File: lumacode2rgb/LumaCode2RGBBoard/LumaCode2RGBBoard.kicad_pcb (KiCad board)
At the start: 2 copper layers, 50 x 60 mm, 74 parts, among them J4 USB_B_Micro, SW1 SW_Push, U1 TVP7002, U10 AP2127K-3.3, U11 74AHC595, U12 74AHC595, U2 AP2127K-3.3, U3 AP2127K-3.3, U4 AP2127K-1.9, U5 AP2127K-1.9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

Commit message: PCB layout
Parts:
- removed C20: 10uF, Capacitor_SMD:C_0805_2012Metric
- added JPICKIT2: Conn_01x02, Connector_PinHeader_2.54mm:PinHeader_1x02_P2.54mm_Vertical, F.Cu at (160.2, 51.4)
- JPICKIT1: value Conn_01x05 -> Conn_01x03; footprint Connector_PinHeader_2.54mm:PinHeader_1x05_P2.54mm_Vertical -> Connector_PinHeader_2.54mm:PinHeader_1x03_P2.54mm_Vertical
- R10, R11, R12, R13, R14, R15, R16, R17, R18, R19, R20, R21, R22, R23, R24, R25, R6, R7, R8, R9: footprint Resistor_SMD:R_0805_2012Metric -> Resistor_SMD:R_0603_1608Metric
- moved C23 131.6 mm to (155.0, 56.8), turned to 180 degrees
- moved C26 120.9 mm to (147.0, 49.8)
- moved R5 110.5 mm to (162.0, 66.4)
- moved C25 109.1 mm to (150.8, 49.2)
- moved U9 106.4 mm to (150.8, 52.5), turned to 90 degrees
- moved C24 96.8 mm to (147.0, 56.5), turned to 180 degrees
- moved R19 92.6 mm to (140.0, 46.0), turned to 90 degrees
- moved R15 92.0 mm to (142.0, 43.0), turned to 180 degrees
- moved R8 89.1 mm to (134.0, 35.5), turned to 180 degrees
- moved R14 88.0 mm to (134.0, 40.5), turned to 180 degrees
- moved R9 86.0 mm to (142.0, 38.0), turned to 180 degrees
- moved R12 85.7 mm to (142.0, 40.5), turned to 180 degrees
- moved R24 85.4 mm to (130.0, 40.5)
- moved R6 85.3 mm to (142.0, 35.5), turned to 180 degrees
- moved R11 84.5 mm to (134.0, 38.0), turned to 180 degrees
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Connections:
- JPICKIT1 pad 1: /Processing/VPP -> /Processing/ICSPCLK
- JPICKIT1 pad 2: +3.3V -> GND
- JPICKIT1 pad 3: GND -> /Processing/ICSPDAT
- R10 pad 2: /Processing/RED -> /Processing/BLUE
- R11 pad 2: /Processing/RED -> /Processing/BLUE
- R17 pad 2: /Processing/BLUE -> /Processing/RED
- R18 pad 2: /Processing/BLUE -> /Processing/RED
- R19 pad 2: /Processing/BLUE -> /Processing/RED
- R20 pad 2: /Processing/BLUE -> /Processing/RED
- R21 pad 2: /Processing/BLUE -> /Processing/RED
- R23 pad 2: /Processing/RED -> /Processing/BLUE
- R25 pad 2: /Processing/BLUE -> /Processing/RED
- R7 pad 2: /Processing/RED -> /Processing/BLUE
- R8 pad 2: /Processing/RED -> /Processing/BLUE
- R9 pad 2: /Processing/RED -> /Processing/BLUE
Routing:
- net +5V: track 0.00 -> 119.8 mm, vias 0 -> 8
- net GND: track 0.00 -> 85.5 mm, vias 0 -> 39
- net Net-(JBOTTOM2-Pad10): track 0.00 -> 51.3 mm, vias 0 -> 2
- net /Input/HSOUT: track 0.00 -> 50.6 mm
- net /Input/VSOUT: track 0.00 -> 50.0 mm
- net /Input/IOVDD: track 0.00 -> 49.3 mm, vias 0 -> 2
- net /Input/AUDIO_LEFT: track 0.00 -> 39.0 mm, vias 0 -> 2
- net Net-(C7-Pad1): track 0.00 -> 38.5 mm
- net /Processing/BLUE: track 0.00 -> 38.1 mm, vias 0 -> 1
- net /Input/SCL: track 0.00 -> 35.6 mm, vias 0 -> 2
- net /Input/SDA: track 0.00 -> 33.5 mm, vias 0 -> 2
- net /Input/AVDD: track 0.00 -> 26.5 mm, vias 0 -> 3
- net /Input/DVDD: track 0.00 -> 24.2 mm, vias 0 -> 2
- net /Processing/GREEN: track 0.00 -> 24.0 mm
- net /Input/A33VDD: track 0.00 -> 21.5 mm
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- added copper zone on B.Cu, net GND
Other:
- outline, holes or cut-outs redrawn

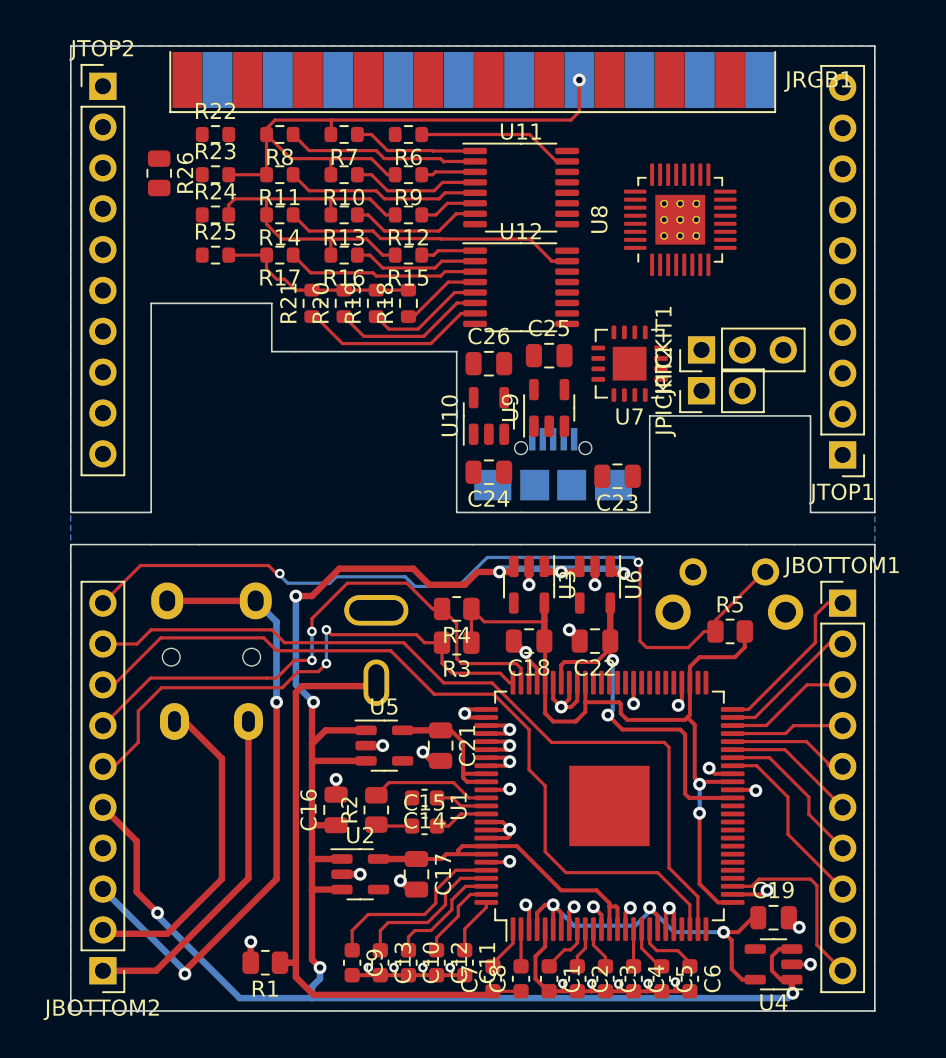
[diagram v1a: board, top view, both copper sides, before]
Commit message: Squeeze all components onto the PCB
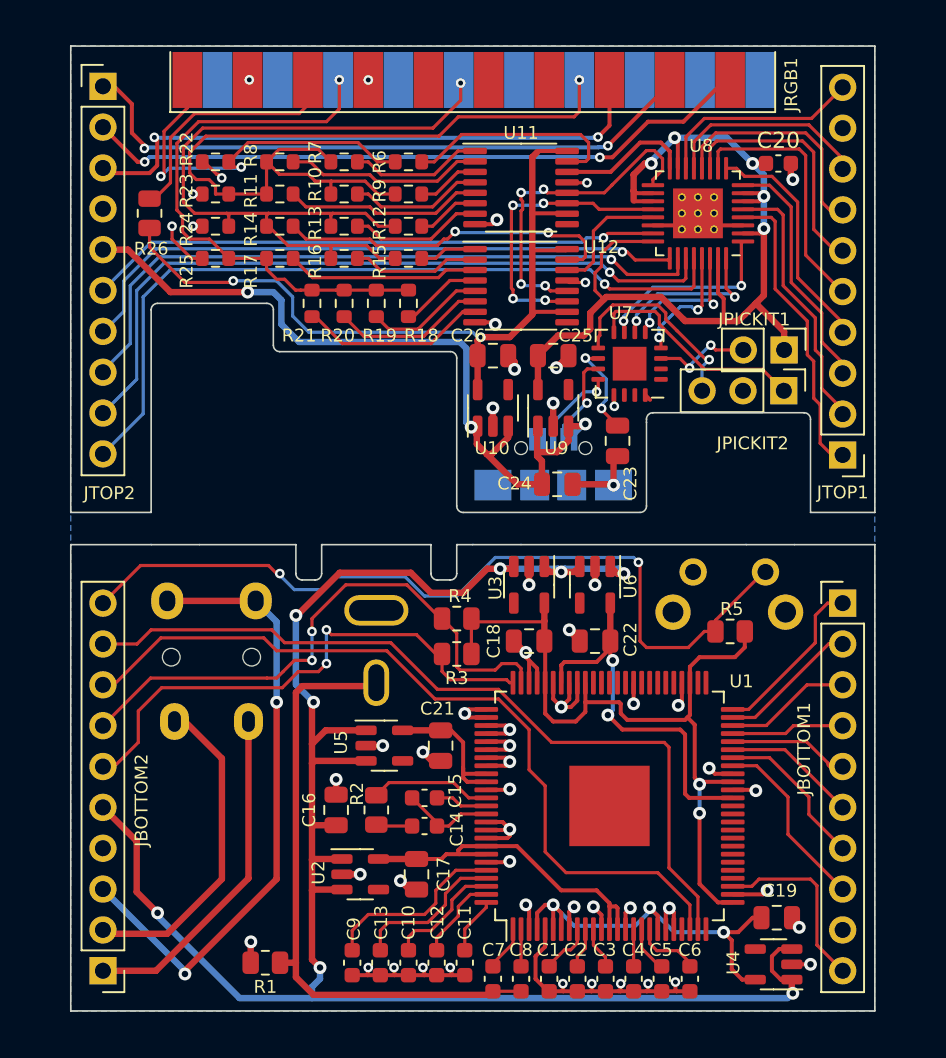
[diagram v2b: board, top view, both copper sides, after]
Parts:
- added C20: 100nF, Capacitor_SMD:C_0603_1608Metric, F.Cu at (165.0, 37.3)
- moved JPICKIT2 5.73 mm to (165.4, 48.9), turned to -90 degrees
- moved JPICKIT1 5.71 mm to (165.3, 51.4), turned to -90 degrees
- moved C24 4.32 mm to (151.2, 57.2), turned to 0 degrees
- moved R26 2.56 mm to (125.9, 40.4)
- moved C23 2.20 mm to (155.0, 54.5), turned to -90 degrees
- moved R22 1.70 mm to (130.0, 37.2)
- moved R6 1.70 mm to (142.0, 37.2)
- moved R7 1.70 mm to (138.0, 37.2)
- moved R8 1.70 mm to (134.0, 37.2)
- moved R10 1.20 mm to (138.0, 39.2)
- moved R11 1.20 mm to (134.0, 39.2)
- moved R23 1.20 mm to (130.0, 39.2)
- moved R9 1.20 mm to (142.0, 39.2)
- moved U8 1.17 mm to (160.0, 40.4), turned to 180 degrees
- moved R12 0.70 mm to (142.0, 41.2)
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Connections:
- C16 pad 1: +5V -> /Input/5V
- JBOTTOM2 pad 5: +5V -> /Input/5V
- U2 pad 1: +5V -> /Input/5V
- U2 pad 3: +5V -> /Input/5V
- U3 pad 1: +5V -> /Input/5V
- U3 pad 3: +5V -> /Input/5V
- U4 pad 1: +5V -> /Input/5V
- U4 pad 3: +5V -> /Input/5V
- U5 pad 1: +5V -> /Input/5V
- U5 pad 3: +5V -> /Input/5V
- U6 pad 1: +5V -> /Input/5V
- U6 pad 3: +5V -> /Input/5V
- U8 pad 10: /Processing/SRCLK -> /Processing/G4
- U8 pad 11: /Processing/SER2 -> /Processing/G5
- U8 pad 12: /Processing/SER1 -> /Processing/G6
- U8 pad 13: /Processing/G0 -> /Processing/G7
- U8 pad 14: /Processing/G1 -> /Processing/CLK
- U8 pad 16: /Processing/G2 -> /Processing/SER1
- U8 pad 17: /Processing/G3 -> /Processing/RCLK
- U8 pad 20: /Processing/G4 -> /Processing/SRCLK
- U8 pad 21: /Processing/CLK -> /Processing/SER2
- U8 pad 23: /Processing/G5 -> /Processing/SDA
- U8 pad 25: /Processing/G6 -> /Processing/SCL
- U8 pad 26: /Processing/G7 -> /Processing/VSOUT
- U8 pad 28: /Processing/VSOUT -> /Processing/BUTTON
- U8 pad 4: /Processing/SDA -> /Processing/G0
- U8 pad 5: /Processing/SCL -> /Processing/G1
- U8 pad 8: /Processing/BUTTON -> /Processing/G2
- U8 pad 9: /Processing/RCLK -> /Processing/G3
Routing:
- net /Input/5V: track 0.00 -> 119.1 mm, vias 0 -> 8
- net +5V: track 119.8 -> 49.0 mm, vias 8 -> 3
- net +3.3V: track 0.00 -> 63.2 mm, vias 0 -> 5
- net /Processing/OUTVDD: track 0.00 -> 50.7 mm, vias 0 -> 2
- net /Processing/BUTTON: track 0.00 -> 48.1 mm, vias 0 -> 1
- net /Processing/HSOUT: track 0.00 -> 45.1 mm, vias 0 -> 1
- net /Processing/AUDIO_RIGHT: track 0.00 -> 42.5 mm, vias 0 -> 2
- net /Processing/VSOUT: track 0.00 -> 42.3 mm, vias 0 -> 1
- net /Processing/AUDIO_GND: track 0.00 -> 39.9 mm, vias 0 -> 2
- net /Processing/SCL: track 0.00 -> 38.8 mm, vias 0 -> 1
- net /Processing/AUDIO_LEFT: track 0.00 -> 37.0 mm, vias 0 -> 2
- net /Processing/SDA: track 0.00 -> 35.7 mm, vias 0 -> 1
- net GND: track 85.5 -> 111.4 mm, vias 39 -> 56
- net /Processing/GREEN: track 24.0 -> 48.9 mm, vias 0 -> 1
- net /Processing/CSYNC: track 0.00 -> 24.2 mm, vias 0 -> 2
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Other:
- outline, holes or cut-outs redrawn
